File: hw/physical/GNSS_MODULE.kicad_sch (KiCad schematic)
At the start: 16 parts, among them J3 Conn_Coaxial, U3 MAX-M8C

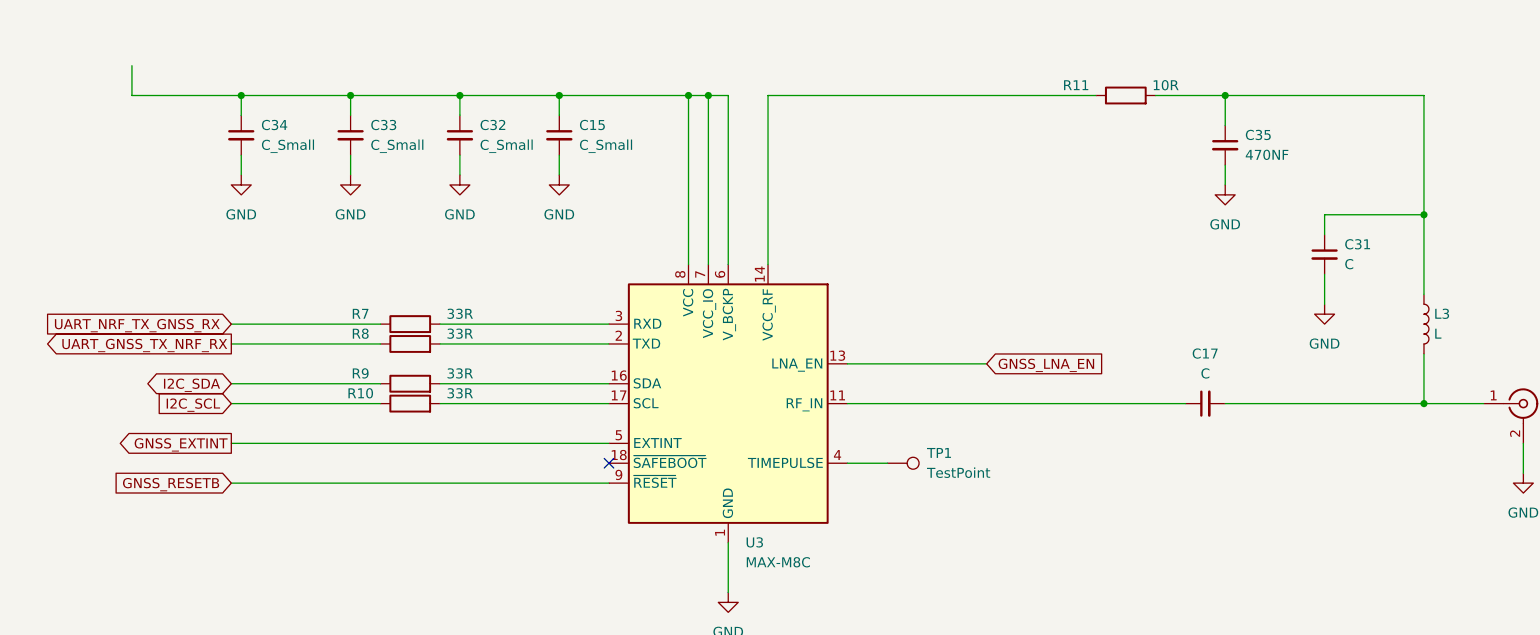
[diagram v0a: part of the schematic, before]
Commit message: - Consolidate POWER and BATTERY pages - Updated 1.8V SYS REG to low Iq option - Replaced LoRA module with SemTech transceiver - Adding latest nRF datasheet
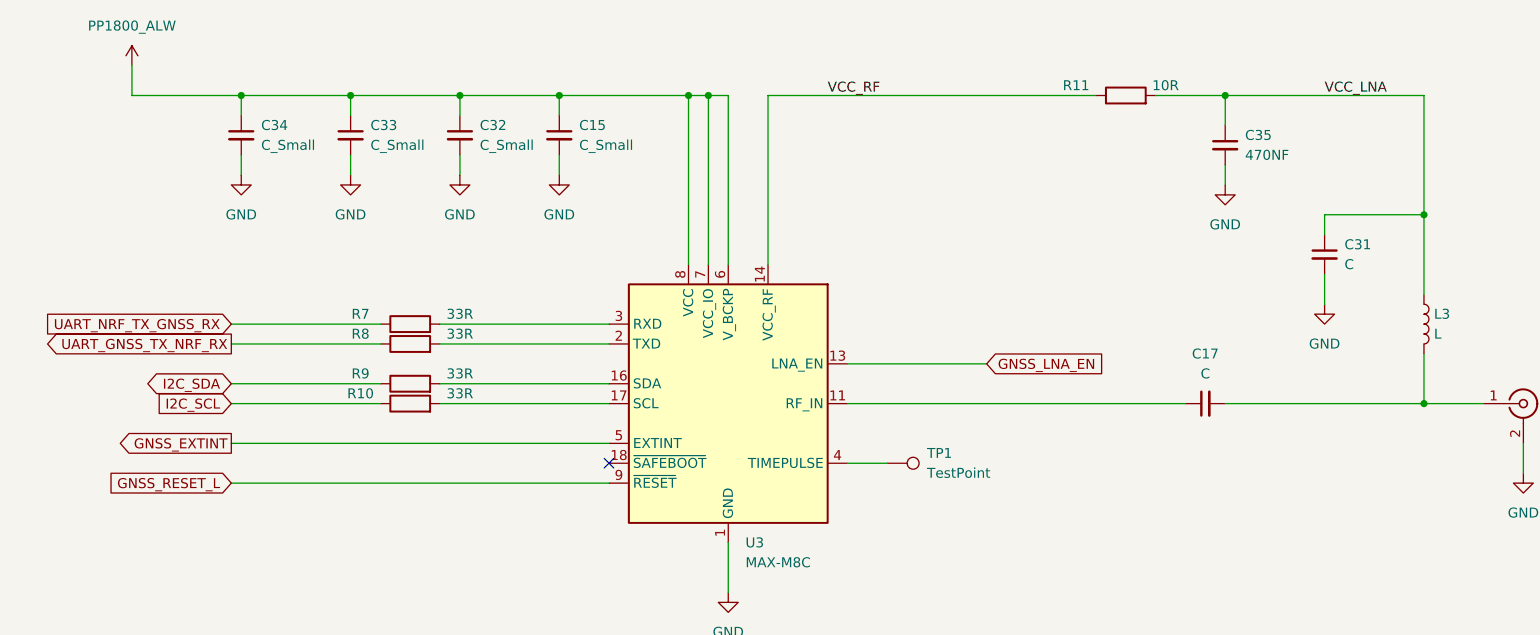
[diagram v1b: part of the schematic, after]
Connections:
- net PP1800_ALW: now reaches C15.1, C32.1, C33.1, C34.1, U3.6 (V_BCKP), U3.7 (VCC_IO), U3.8 (VCC)
- net VCC_LNA: now reaches C31.1, C35.1, L3.1, R11.2
- net VCC_RF: now reaches R11.1, U3.14 (VCC_RF)
- net GNSS_RESETB renamed GNSS_RESET_L
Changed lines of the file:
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@@
+		)
+	)
+	(label "VCC_LNA"
+		(at 279.4 88.9 0)
+		(fields_autoplaced yes)
+		(effects
+			(font
+				(size 1.27 1.27)
+			)
+			(justify left bottom)
+		)
+	)
+	(label "VCC_RF"
+		(at 215.9 88.9 0)
+		(fields_autoplaced yes)
+		(effects
+			(font
+				(size 1.27 1.27)
+			)
+			(justify left bottom)
 		)
 	)
@@
 		)
 	)
-	(global_label "GNSS_RESETB"
+	(global_label "GNSS_RESET_L"
 		(shape input)
 		(at 139.7 138.43 180)
@@
 		)
 		(property "Intersheetrefs" "${INTERSHEET_REFS}"
-			(at 123.7126 138.43 0)
+			(at 122.9869 138.43 0)
 			(effects
 				(font
@@
 		)
 	)
+	(netclass_flag ""
+		(length 2.54)
+		(shape round)
+		(at 228.6 88.9 0)
+		(fields_autoplaced yes)
+		(effects
+			(font
+				(size 1.27 1.27)
+			)
+			(justify left bottom)
+		)
+		(property "Netclass" "Power"
+			(at 229.2985 86.36 0)
+			(effects
+				(font
+					(size 1.27 1.27)
+					(italic yes)
+				)
+				(justify left)
+			)
+		)
+	)
+	(netclass_flag ""
+		(length 2.54)
+		(shape round)
+		(at 271.78 88.9 0)
+		(fields_autoplaced yes)
+		(effects
+			(font
+				(size 1.27 1.27)
+			)
+			(justify left bottom)
+		)
+		(property "Netclass" "Power"
+			(at 272.4785 86.36 0)
+			(effects
+				(font
+					(size 1.27 1.27)
+					(italic yes)
+				)
+				(justify left)
+			)
+		)
+	)
 	(symbol
 		(lib_id "power:GND")
@@
 					(unit 1)
 				)
+			)
+		)
+	)
+	(symbol
+		(lib_id "power:VCC")
+		(at 127 85.09 0)
+		(unit 1)
+		(exclude_from_sim no)
+		(in_bom yes)
+		(on_board yes)
+		(dnp no)
+		(fields_autoplaced yes)
+		(property "Reference" "#PWR0401"
+			(at 127 88.9 0)
+			(effects
+				(font
+					(size 1.27 1.27)
+				)
+				(hide yes)
+			)
+		)
+		(property "Value" "PP1800_ALW"
+			(at 127 80.01 0)
+			(effects
+				(font
+					(size 1.27 1.27)
+				)
+			)
+		)
+		(property "Footprint" ""
+			(at 127 85.09 0)
+			(effects
+				(font
+					(size 1.27 1.27)
+				)
+				(hide yes)
+			)
+		)
+		(property "Datasheet" ""
+			(at 127 85.09 0)
+			(effects
+				(font
+					(size 1.27 1.27)
+				)
+				(hide yes)
+			)
+		)
+		(property "Description" "Power symbol creates a global label with name \"VCC\""
+			(at 127 85.09 0)
+			(effects
+				(font
+					(size 1.27 1.27)
+				)
+				(hide yes)
+			)
+		)
+		(pin "1"
+		)
+		(instances
+			(project "lora_radio_lp"
+				(path "/fff85bc4-e8ec-4b5d-b2e2-83ecb397a864/43b1fc22-b706-4706-a6f5-d4b7f0f9014a"
+					(reference "#PWR0401")
+					(unit 1)
+				)

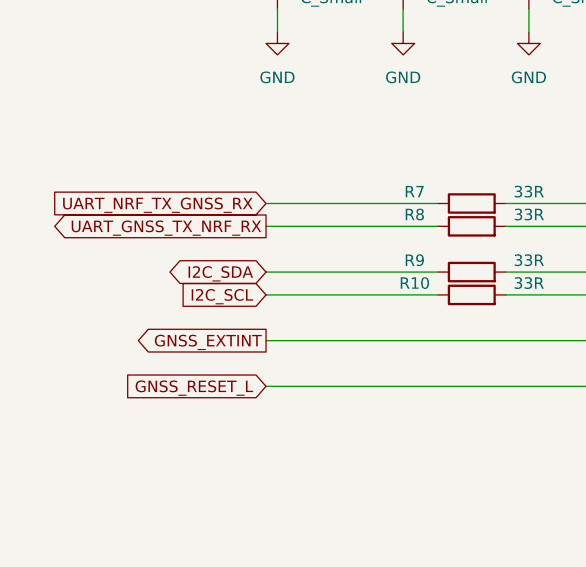
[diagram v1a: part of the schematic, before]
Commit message: Adding nRF54L10 schematic library component. Redrew MCU page with nRF54L10 and rearranged or changed net labels and global labels.
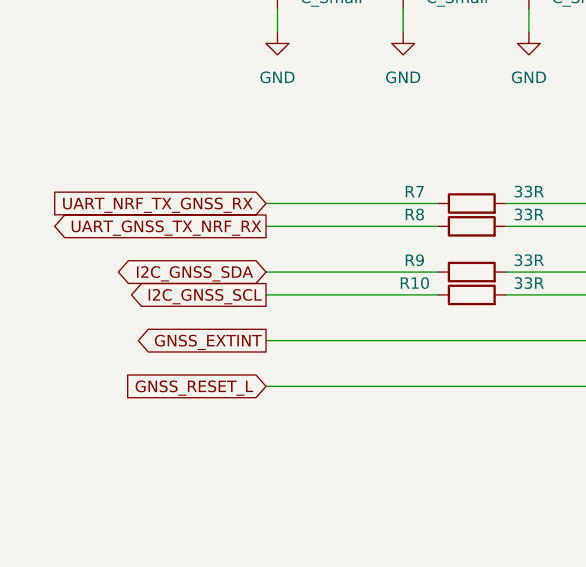
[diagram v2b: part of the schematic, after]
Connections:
- net I2C_SCL renamed I2C_GNSS_SCL
- net I2C_SDA renamed I2C_GNSS_SDA
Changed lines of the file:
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@@
+		)
+	)
+	(global_label "I2C_GNSS_SDA"
+		(shape bidirectional)
+		(at 139.7 125.73 180)
+		(fields_autoplaced yes)
+		(effects
+			(font
+				(size 1.27 1.27)
+			)
+			(justify right)
+		)
+		(property "Intersheetrefs" "${INTERSHEET_REFS}"
+			(at 121.9964 125.73 0)
+			(effects
+				(font
+					(size 1.27 1.27)
+				)
+				(justify right)
+				(hide yes)
+			)
+		)
+	)
+	(global_label "I2C_GNSS_SCL"
+		(shape output)
+		(at 139.7 128.27 180)
+		(fields_autoplaced yes)
+		(effects
+			(font
+				(size 1.27 1.27)
+			)
+			(justify right)
+		)
+		(property "Intersheetrefs" "${INTERSHEET_REFS}"
+			(at 123.1682 128.27 0)
+			(effects
+				(font
+					(size 1.27 1.27)
+				)
+				(justify right)
+				(hide yes)
+			)
 		)
 	)
@@
 			(effects
 				(font
-					(size 1.27 1.27)
-				)
-				(justify right)
-				(hide yes)
-			)
-		)
-	)
-	(global_label "I2C_SDA"
-		(shape bidirectional)
-		(at 139.7 125.73 180)
-		(fields_autoplaced yes)
-		(effects
-			(font
-				(size 1.27 1.27)
-			)
-			(justify right)
-		)
-		(property "Intersheetrefs" "${INTERSHEET_REFS}"
-			(at 127.9835 125.73 0)
-			(effects
-				(font
-					(size 1.27 1.27)
-				)
-				(justify right)
-				(hide yes)
-			)
-		)
-	)
-	(global_label "I2C_SCL"
-		(shape input)
-		(at 139.7 128.27 180)
-		(fields_autoplaced yes)
-		(effects
-			(font
-				(size 1.27 1.27)
-			)
-			(justify right)
-		)
-		(property "Intersheetrefs" "${INTERSHEET_REFS}"
-			(at 129.1553 128.27 0)
-			(effects
-				(font
